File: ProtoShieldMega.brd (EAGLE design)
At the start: 81.3 x 53.3 mm, 32 parts, among them J1 Digital_0_7, J2 Analog, J3 Digital_8_13, J4 Analog, J5 Digital_0_7, J6 Digital_22_36, J7 Digital_23_37, J8 Digital_38_52, J9 Digital_39_53

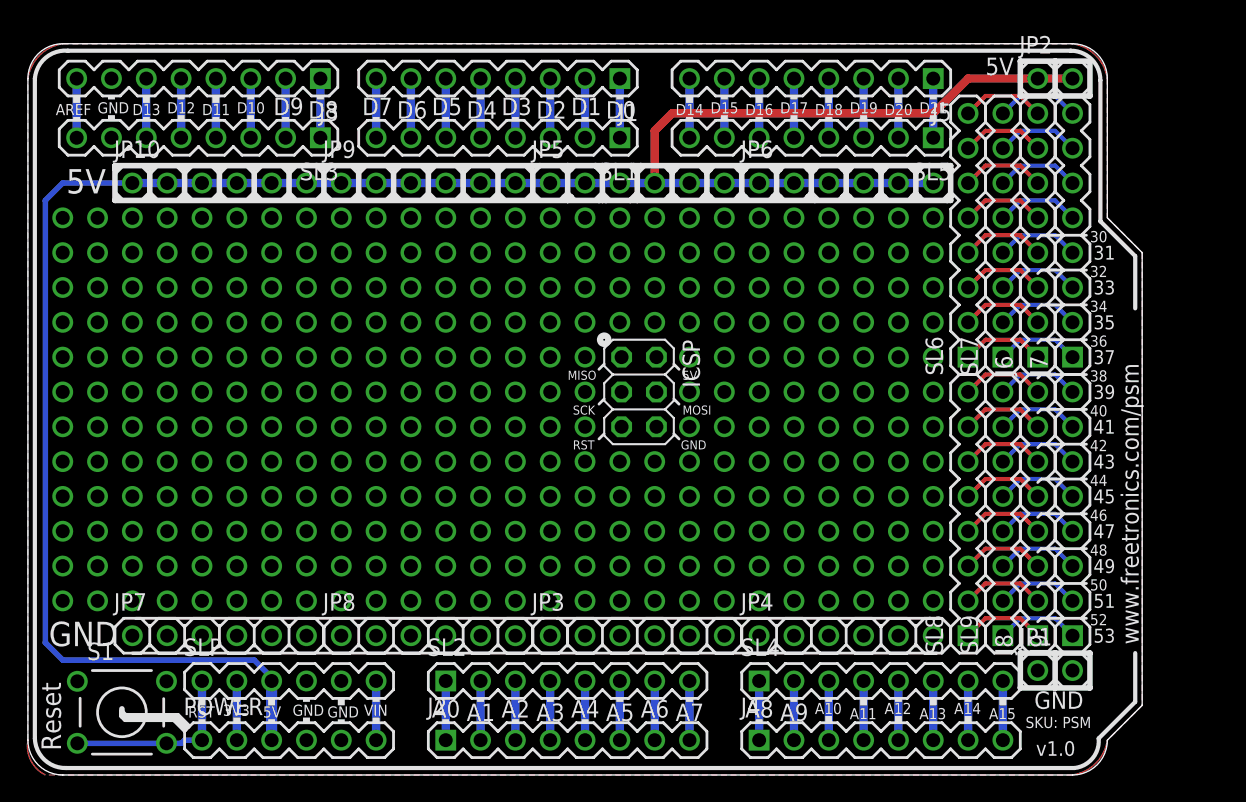
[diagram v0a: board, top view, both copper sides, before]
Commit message: Update for Arduino R3 headers
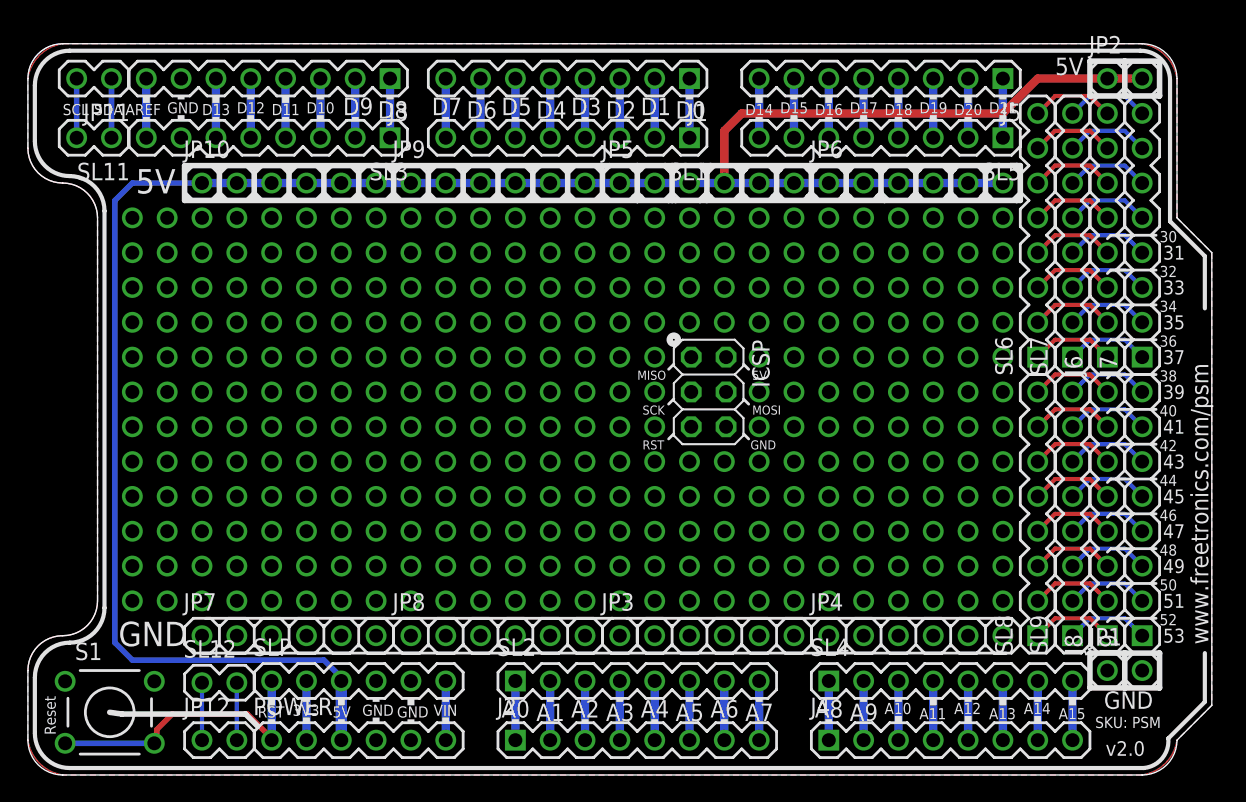
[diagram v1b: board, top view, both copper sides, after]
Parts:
- added JP11: i2c, freetronics:1X02
- added JP12: IOREF, freetronics:1X02
- added SL11, SL12: (no value), freetronics:1X02
- moved J2 5.08 mm to (35.6, 2.54)
- moved J3 5.08 mm to (26.4, 50.8)
- moved JP8 5.08 mm to (27.9, 10.2)
- moved JP9 5.08 mm to (27.9, 43.2)
- moved POWER 5.08 mm to (17.8, 2.54)
- moved SL2 5.08 mm to (35.6, 6.86)
- moved SL3 5.08 mm to (26.4, 46.5)
- moved SLP 5.08 mm to (17.8, 6.86)
- moved JP10 5.08 mm to (12.7, 43.2)
- moved JP7 5.08 mm to (12.7, 10.2)
- moved ICSP 5.08 mm to (49.7, 27.9)
- moved J1 5.08 mm to (48.3, 50.8)
- moved J4 5.08 mm to (58.4, 2.54)
- moved J5 5.08 mm to (71.1, 50.8)
- moved J6 5.08 mm to (78.7, 30.5)
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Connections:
- new net IOREF: JP12.2, SL12.2
- new net NC: JP12.1, SL12.1
- new net SCL: JP11.2, SL11.2
- new net SDA: JP11.1, SL11.1
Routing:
- net RESET: track 13.5 -> 21.6 mm
- net SDA: track 0.00 -> 4.32 mm
- net SCL: track 0.00 -> 4.32 mm
- net NC: track 0.00 -> 4.19 mm
- net IOREF: track 0.00 -> 4.19 mm
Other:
- board size 81.3 x 53.3 mm -> 86.4 x 53.3 mm
- board text added: "(C) 2013"
- board text added: "ProtoShield Mega R3"
- board text added: "SCL"
- board text added: "SDA"
- board text added: "v2.0"
- board text removed: "(C) 2012"
- board text removed: "ProtoShield Mega"
- board text removed: "v1.0"
